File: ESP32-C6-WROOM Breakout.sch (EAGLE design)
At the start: 65 parts, among them J10 HP I2C, J11 LP I2C, J2 LP I2C, P1 GPIO-A2, P10 LP_I2C, P11 LiPo In, P2 GPIO-A1, P3 ADC, P4 O/P DRV, P5 CTRL, P6 HP_UART, P7 HP_I2C, P8 B2B-PH-K, P9 B2B-PH-K, U1 AP2112K-3.3TRG1, U2 ESP32-C6-WROOM-1-N4, U3 AP2112K-3.3TRG1LONG_PADS

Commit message: gitignore + WIP (close to candidate v1)
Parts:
- removed Q1, Q2, Q3, Q4: (no value), Master 2016:MOSFET-P-SOT23
- removed U1: AP2112K-3.3TRG1, AP2112K-3.3TRG1:AP2112K-3.3TRG1
- added J3: HP_UART, Connector:HEADER-5P-2.54
- added Q6, Q7, Q8: (no value), Master 2016:FDN338P_PMOSSOT23_LONG
- U3: value AP2112K-3.3TRG1LONG_PADS -> AP2112
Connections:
- net GND: now also J3.1; no longer U1.GND
- net GPIO22: now also Q8.G; no longer Q2.G
- net GPIO23: now also Q6.G; no longer Q4.G
- net LP_GPIO4: now also Q7.G; no longer Q3.G
- net LP_GPIO5: no longer Q1.G
- net N$12: now also Q7.D; no longer Q3.D
- net N$13: no longer U1.VOUT
- net N$15: now also Q6.D; no longer Q4.D
- net N$7: no longer Q1.D
- net RX: now also J3.4
- net TX: now also J3.5
- net UART_VCC: now also J3.3, Q8.D; no longer Q2.D
- net VCC: now also Q6.S, Q7.S, Q8.S; no longer Q1.S, Q2.S, Q3.S, Q4.S
- net VIN: no longer U1.EN, U1.VIN
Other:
- moved on the sheet: C6, C7, J10, P7, Q5, U3

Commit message: WIP getting there
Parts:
- added P12: Pwr Out, con-jst-ph:B3B-PH-K
- added P13: (no value), Master 2016:HEADER-1X2PPTH
- added Q1: FDN338P, Master 2016:FDN338P_PMOSSOT23_LONG
- added R12, R13, R14, R15, R21: (no value), Master 2016:R-EU_
- added R16, R17, R18, R19: 4k7, Master 2016:R-EU_
- added R20: 10k, Master 2016:R-EU_
- BAT1: value (none) -> 2-1775485-1
- C1, C2: value (none) -> 18p
- C3: value (none) -> 10u
- JP10: value BOOT -> (none)
- JP12: value (none) -> UART Vcc; device Master 2016:HEADER-1X2PPTH -> Connector:HEADER-3P-2.54
- JP8: value (none) -> BOOT
- JP9: value (none) -> I_measure
- P1: value GPIO-A2 -> LP_I2C; device con-jst-eh:B3B-EH-A -> con-jst-eh:B4B-EH-A
- P10: value LP_I2C -> Pwr Sw 23; device con-jst-eh:B4B-EH-A -> con-jst-ph:B2B-PH-K
- P2: value GPIO-A1 -> HP_I2C; device con-jst-eh:B5B-EH-A -> con-jst-eh:B4B-EH-A
- P3: value ADC -> CTRL
- P5: value CTRL -> ADC; device con-jst-eh:B3B-EH-A -> con-jst-eh:B4B-EH-A
- P6: value HP_UART -> GPIO-A1; device con-jst-eh:B4B-EH-A -> con-jst-eh:B5B-EH-A
- P7: value HP_I2C -> HP_UART
- P8: value B2B-PH-K -> GPIO-A2; device con-jst-ph:B2B-PH-K -> con-jst-eh:B3B-EH-A
- P9: value B2B-PH-K -> Pwr Sw 22
- Q5, Q6, Q7, Q8: value (none) -> FDN338P
- R3, R5, R6, R8: value (none) -> 10k
- X1: value (none) -> CFS-20632768EZFB
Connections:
- new net LP_GPIO6: U2.IO6
- new net LP_GPIO7: U2.IO7
- new net N$9: P5.4, Q1.D
- new net PWR_SW_22: JP12.P$1, JP6.2, P9.2, Q8.D
- net ADC: now also P5.2; no longer P3.2
- net GND: now also JP2.2, JP3.2, P1.2, P10.1, P12.1, P2.2, P7.1; no longer JP10.2, JP7.2, P1.1, P10.2, P2.1, P7.2
- net GPIO10: now also P2.3, R18.1; no longer P7.3
- net GPIO11: now also P2.4, R19.1; no longer P7.4
- net GPIO15_R: now also JP10.2, P3.2; no longer JP11.2, P5.2
- net GPIO18: now also P6.2; no longer P2.2
- net GPIO19: now also JP2.1, P6.3; no longer JP7.1, P2.3
- net GPIO20: now also JP3.1, P6.4; no longer JP8.1, P2.4
- net GPIO21: now also P6.5, R2.1; no longer P2.5
- net GPIO22: now also P8.3, R15.1, R15.2; no longer P1.3, R2.1
- net GPIO23: now also P8.2, R14.1, R14.2; no longer P1.2
- net GPIO6: now also P1.4, Q1.G, R16.2, R20.1, R21.1, R21.2; no longer P10.4, U2.IO6
- net GPIO7: now also P1.3, R17.2; no longer P10.3, U2.IO7
- net GPIO8: now also P13.1; no longer JP6.1
- net GPIO9: now also P13.2; no longer JP6.2
- net LP_GPIO3: now also P3.3; no longer P5.3
- net LP_GPIO4: now also R13.1, R13.2
- net LP_GPIO5: now also JP5.2, R12.1, R12.2; no longer JP2.2
- net LP_GPIO5_P: now also JP5.1; no longer JP2.1
- net N$1: now also JP8.1; no longer JP10.1
- net N$10: now also JP11.2; no longer JP12.2
- net N$11: now also JP11.1; no longer JP12.1
- net N$15: now also JP7.2, P10.2; no longer JP5.2, P9.2
- net N$8: now also JP10.1; no longer JP11.1
- net RX: now also P7.3; no longer P6.3
- net TX: now also P7.2; no longer P6.2
- net UART_VCC: now also JP12.P$2, P7.4; no longer JP3.2, P6.4, P8.2, Q8.D
- net VCC: now also JP12.P$3, JP6.1, JP7.1, P1.1, P12.2, P2.1, P5.3, Q1.S, R16.1, R17.1, R18.2, R19.2, R20.2; no longer JP3.1, JP5.1, P10.1, P3.3, P7.1
- net VIN: now also P12.3
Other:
- note added: "Alt MIC5504"
- note added: "Cut trace if gate series resistors R12-R14 required"
- note added: "For CR2032 coin cell"
- note added: "R1, R2 chosen to suit load I"
- note added: "R16-R19 I2C pull-ups Use if required. Typically 3k9 or 4k7"
- note added: "R4, R7 to suit load I"
- note added: "Vcc control for ADC and LP_I2C are mutually incompatible"
- note added: "see also LED1"
- note added: "see also P5"
- moved on the sheet: BAT1, C3, C6, C7, C8, D1, D3, J1, J10, J11, J2, J3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

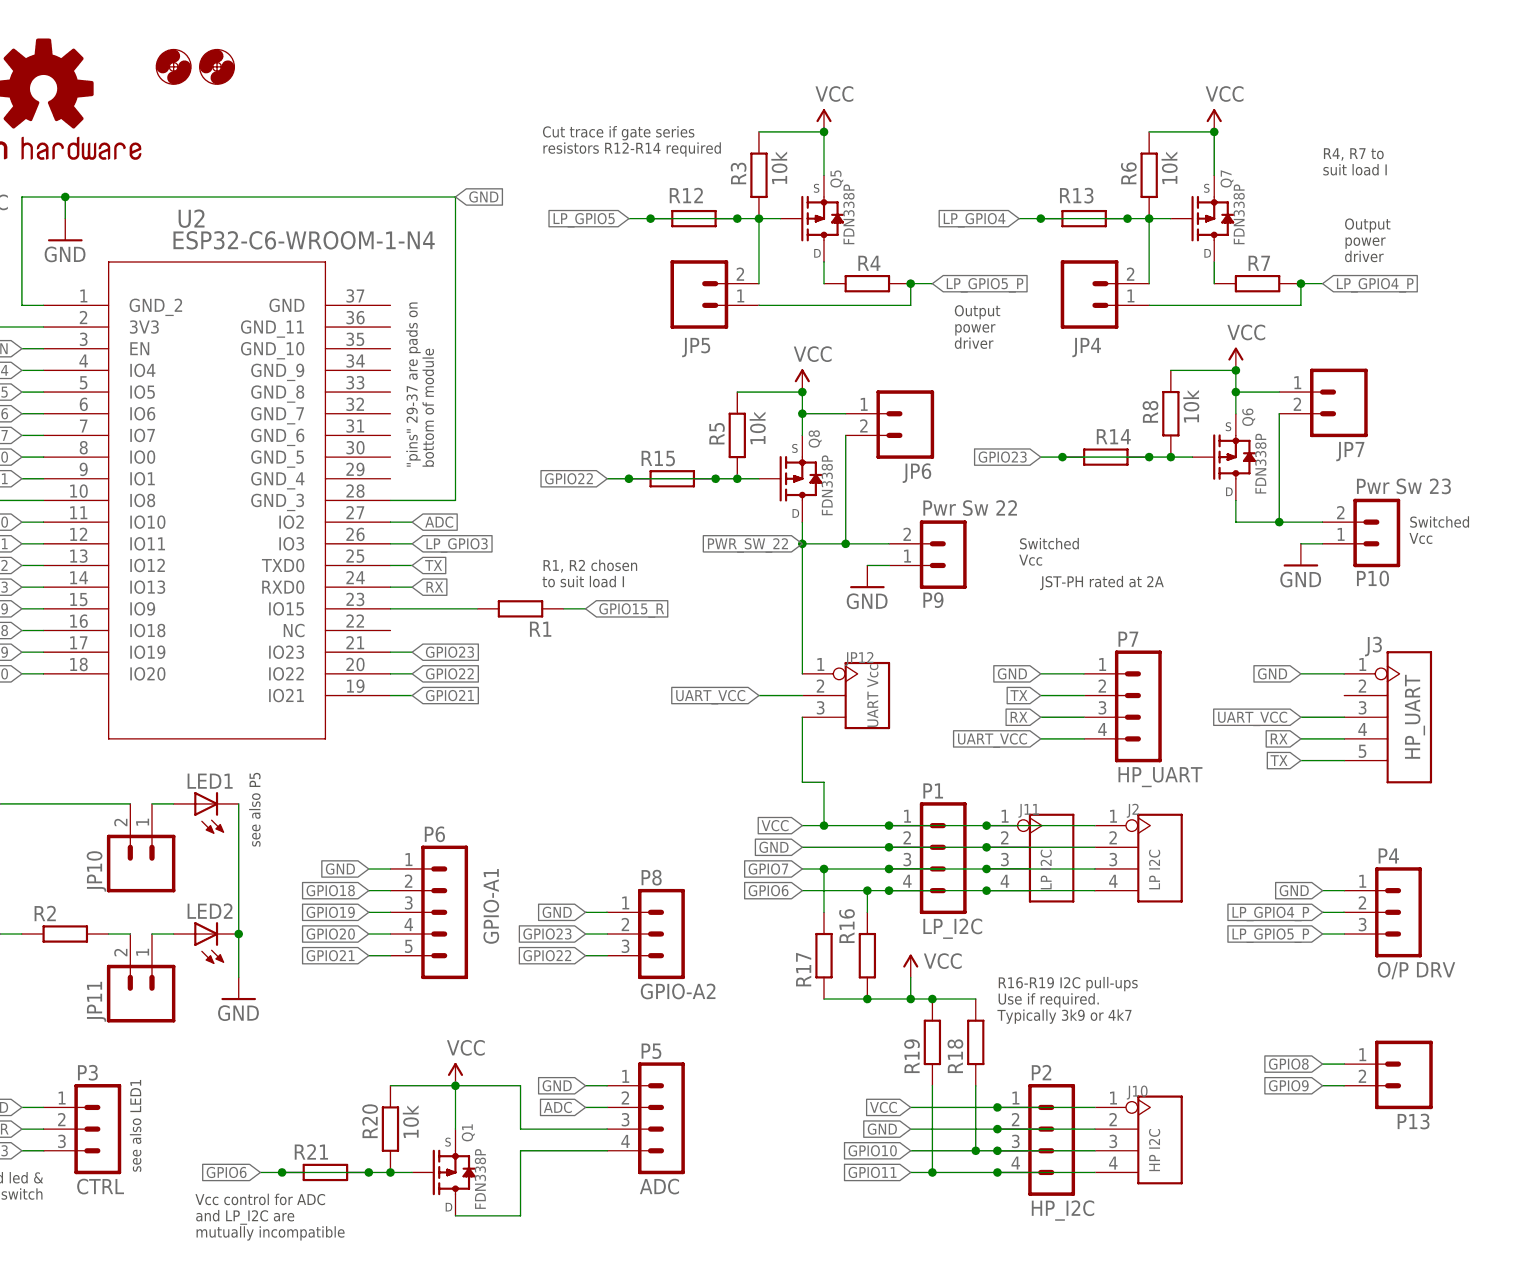
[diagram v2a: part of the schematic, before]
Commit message: move ADC and add o/p drive caps
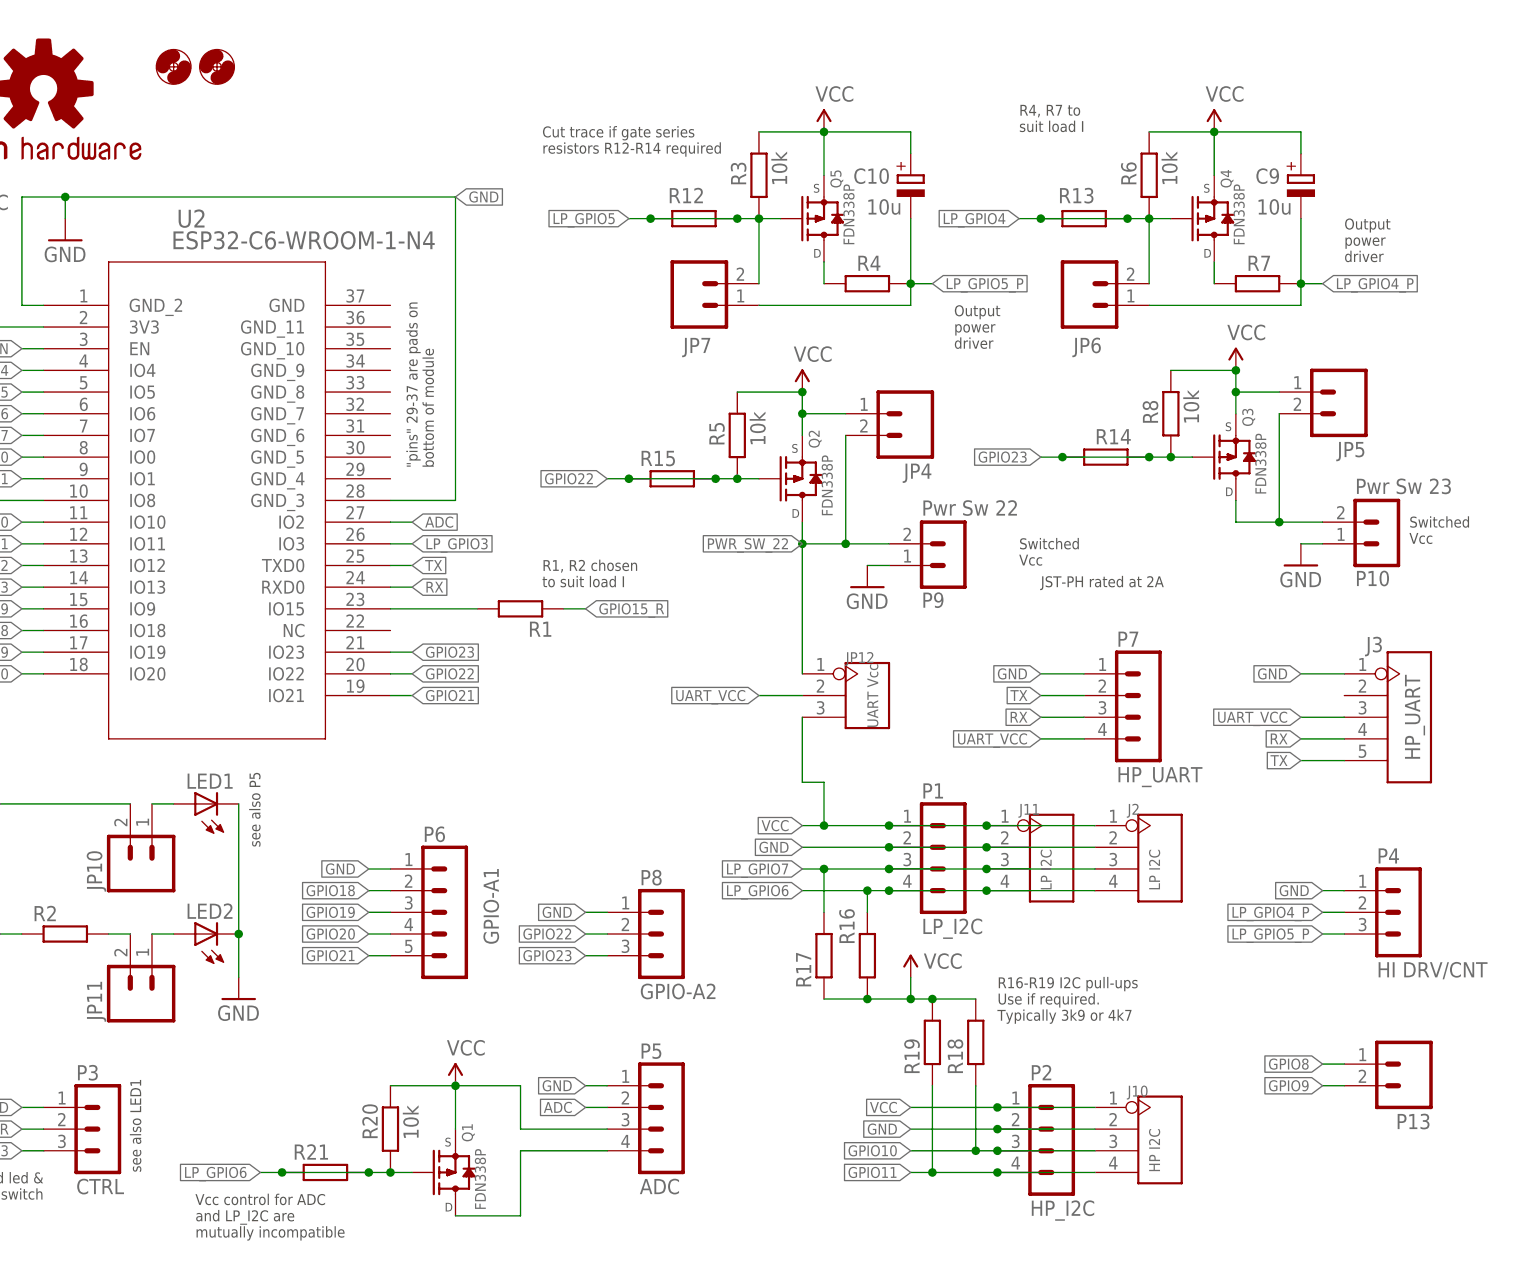
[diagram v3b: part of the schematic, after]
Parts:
- added C10, C9: 10u, Master 2016:CPOL-EUE2.5-5**10UF
- P4: value O/P DRV -> HI DRV/CNT
- renumbered Q6 to Q3, Q7 to Q4, Q8 to Q2
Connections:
- net N$16 renamed GPIO15
- removed net GPIO6: J11.P$4, J2.P$4, P1.4, Q1.G, R16.2, R20.1, R21.1, R21.2
- removed net GPIO7: J11.P$3, J2.P$3, P1.3, R17.2
- net GPIO22: now also P8.2; no longer P8.3
- net GPIO23: now also P8.3; no longer P8.2
- net LP_GPIO4: now also JP6.2; no longer JP4.2
- net LP_GPIO4_P: now also C9.-, JP6.1; no longer JP4.1
- net LP_GPIO5: now also JP7.2; no longer JP5.2
- net LP_GPIO5_P: now also C10.-, JP7.1; no longer JP5.1
- net LP_GPIO6: now also J11.P$4, J2.P$4, P1.4, Q1.G, R16.2, R20.1, R21.1, R21.2
- net LP_GPIO7: now also J11.P$3, J2.P$3, P1.3, R17.2
- net N$15: now also JP5.2; no longer JP7.2
- net PWR_SW_22: now also JP4.2; no longer JP6.2
- net VCC: now also C10.+, C9.+, JP4.1, JP5.1; no longer JP6.1, JP7.1
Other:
- moved on the sheet: JP4, JP5, JP6, JP7

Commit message: close to v1 rev
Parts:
- removed Q5: FDN338P, Master 2016:FDN338P_PMOSSOT23_LONG
- added D4: SL115B, Master 2016:DIODE-SCHOTTKY
- added J4, J5: (no value), Connector:HEADER-1P-35
- added JP13: PS Src, Connector:HEADER-3P-2.54
- added JP14: I_measure, Master 2016:HEADER-1X2PPTH
- added P14: Backup, con-jst-ph:B2B-PH-K
- C10: device Master 2016:CPOL-EUE2.5-5**10UF -> Master 2016:C-EU1206
- C3, C9: value 10u -> 100n; device Master 2016:CPOL-EUE2.5-5**10UF -> Master 2016:C-EU1206
- C6: value 100n -> 1u
- C7: value 10u -> 1u; device Master 2016:CPOL-EUE2.5-5**10UF -> Master 2016:C-EU1206
- C8: value 100n -> 10u
- J2: value LP I2C -> HP I2C
- JP3: value (none) -> BOOT
- JP8: value BOOT -> (none)
- JP9: value I_measure -> (none)
- P10: device con-jst-ph:B2B-PH-K -> con-jst-ph:B3B-PH-K
- P5: device con-jst-eh:B4B-EH-A -> con-jst-eh:B3B-EH-A
- P6: device con-jst-eh:B5B-EH-A -> con-jst-eh:B6B-EH-A
- R20: value 10k -> 2k2
- R21: value (none) -> 1k
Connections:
- new net N$14: JP13.P$3, P10.3
- new net N$16: J4.1, JP1.1
- new net N$2: D2.A, P11.1
- new net N$5: JP13.P$2, JP5.1, Q1.S, R8.2
- net ADC: now also C9.1, R20.1, R21.1
- net GND: now also C10.1, C3.2, C7.2, C9.2, P10.2, P11.2, P12.2, P14.2, P9.2, R20.2; no longer C3.-, C7.-, JP8.2, P10.1, P11.1, P12.1, P9.1
- net GPIO10: now also J2.P$3
- net GPIO11: now also J2.P$4
- net GPIO18: no longer JP1.1
- net GPIO19: no longer JP2.1
- net GPIO20: no longer JP3.1
- net GPIO23: now also Q1.G; no longer Q3.G
- net LP_GPIO4: now also Q3.G; no longer Q4.G
- net LP_GPIO4_P: now also JP8.2; no longer C9.-
- net LP_GPIO5: now also Q4.G; no longer Q5.G
- net LP_GPIO5_P: now also JP9.2; no longer C10.-
- net LP_GPIO6: no longer J2.P$4, Q1.G, R20.1, R21.1, R21.2
- net LP_GPIO7: no longer J2.P$3
- net N$1: now also JP3.1; no longer JP8.1
- net N$12: now also JP8.1, Q3.D; no longer Q4.D
- net N$13: now also C7.1, D3.C, JP14.1; no longer C6.1, C7.+, JP9.1
- net N$15: now also P10.1, Q1.D; no longer P10.2, Q3.D
- net N$4: now also D4.A, P14.1; no longer D2.A, P11.2
- net N$7: now also JP9.1, Q4.D; no longer Q5.D
- net N$9: now also J5.1, JP2.1; no longer P5.4, Q1.D
- net PWR_SW_22: now also P9.1; no longer P9.2
- net VCC: now also C10.2, C3.1, C8.1, JP13.P$1, JP14.2, P12.1, P6.6; no longer C10.+, C9.+, JP5.1, JP9.2, P12.2, Q1.S, Q5.S, R20.2, R8.2
- net VIN: now also C6.1, D4.C, R21.2; no longer C3.+, C8.1, D3.C
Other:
- note added: "Allow for an external Pwr src to be switched"
- note added: "C8 is decoupling for one/both"
- note added: "Config Jumpers not attached - use flying wires to link to GPIO"
- note added: "Output power driver. Not meant for PWM (MOSFET gate driver better at high freq)"
- note added: "P14 is option for e.g. a LiSOCl2 cell for when coin cell is insufficient."
- note added: "R4, R7 to suit load I. Parallel JP to allow easy changing."
- note added: "see also P3"
- note removed: "Config Jumpers"
- note removed: "Output power driver"
- note removed: "R4, R7 to suit load I"
- note removed: "Vcc control for ADC and LP_I2C are mutually incompatible"
- note removed: "see also P5"
- moved on the sheet: C6, C8, D3, J10, J2, J3, JP3, JP5, JP6, JP7, JP8, JP9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

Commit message: v1.1 essentially completed
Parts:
- removed JP10, JP4: (no value), Master 2016:HEADER-1X2PPTH
- removed JP13: PS Src, Connector:HEADER-3P-2.54
- removed Q4: FDN338P, Master 2016:FDN338P_PMOSSOT23_LONG
- added R22: 22k, Master 2016:R-EU_
- added U1: 74LVC1G3157, ESP32 Projects:SN74LVC1G3157DBVR
- added U4, U5: MIC2005A-1YM5, ESP32 Projects:MIC2005A-1YM5-TRSOT-23-5_M5_MCH-M
- added USB1: (no value), Master 2016:USB-FCI_SMD_LONG***
- J1: value (none) -> HP I2C; device Master 2016:USB-FCI_SMD*** -> Connector:HEADER-4P-80/40MIL
- J10: value HP I2C -> (none); device Connector:HEADER-4P-80/40MIL -> Master 2016:HEADER-1X2PPTH
- P10: device con-jst-ph:B3B-PH-K -> con-jst-ph:B2B-PH-K
- P11: value LiPo In -> Battery
- P13: value (none) -> Pwr Sw 22; device Master 2016:HEADER-1X2PPTH -> con-jst-ph:B2B-PH-K
- P5: value ADC -> ADC (ext batt)
- P9: value Pwr Sw 22 -> GPIO-B; device con-jst-ph:B2B-PH-K -> con-jst-eh:B4B-EH-A
- R15: value (none) -> 10k
- R20: value 2k2 -> 10k
- R21: value 1k -> 22k
- U2: value ESP32-C6-WROOM-1-N4 -> ESP32-C6-WROOM-1-N4LONG; device SMD Stamp Modules:ESP32-C6-WROOM-1-N4 -> SMD Stamp Modules:ESP32-C6-WROOM-1-N4LONG
- U3: value AP2112 -> RT9080-33
- renumbered JP12 to J12, JP14 to J14, JP6 to J6, JP7 to J7, JP8 to J8, JP9 to J9
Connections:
- removed net N$14: JP13.P$3, P10.3
- new net ADC_EXT: P5.2, U1.B1
- new net VIN_DIV: R20.1, R21.1, U1.B2
- net ADC: now also U1.A; no longer P5.2, R20.1, R21.1
- net GND: now also J1.P$2, P10.1, P11.1, P13.1, P14.1, R15.2, R5.2, U1.GND, U4.GND, U5.GND, USB1.GND; no longer J1.GND, J10.P$2, P10.2, P11.2, P14.2
- net GPIO10: now also J1.P$3; no longer J10.P$3
- net GPIO11: now also J1.P$4; no longer J10.P$4
- net GPIO12: now also USB1.D-; no longer J1.D-
- net GPIO13: now also USB1.D+; no longer J1.D+
- net GPIO15: now also R5.1, U1.S, U5.ENABLE
- net GPIO15_R: now also J10.2; no longer JP10.2
- net GPIO22: now also U4.ENABLE; no longer Q2.G, R15.2, R5.1
- net GPIO8: now also P9.3; no longer P13.1
- net GPIO9: now also P9.1; no longer P13.2
- net LP_GPIO3: now also R22.1
- net LP_GPIO4: now also P5.3, Q2.G; no longer Q3.G
- net LP_GPIO5: now also Q3.G; no longer Q4.G
- net N$12: now also Q2.D; no longer Q3.D
- net N$15: now also R21.2, U5.VOUT; no longer JP5.2, P10.1, Q1.D
- net N$2: now also P11.2; no longer P11.1
- net N$3: now also USB1.VBUS; no longer J1.VBUS
- net N$4: now also P14.2; no longer P14.1
- net N$5: now also JP5.2, P10.2, Q1.D; no longer JP13.P$2, JP5.1, Q1.S, R8.2
- net N$7: now also Q3.D; no longer Q4.D
- net N$8: now also J10.1; no longer JP10.1
- net PWR_SW_22: now also P13.2, U4.VOUT; no longer JP4.2, P9.1, Q2.D
- net VCC: now also J1.P$1, JP5.1, P9.4, Q1.S, R22.2, R8.2, U1.VCC, U4.VIN; no longer J10.P$1, JP13.P$1, JP4.1, P5.3, Q4.S, R5.2
- net VIN: now also U5.VIN; no longer R21.2
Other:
- note added: "Alt MIC5504 or AP2112 (but these have higher I_q)"
- note removed: "Allow for an external Pwr src to be switched"
- note removed: "Alt MIC5504"
- moved on the sheet: C10, P11, P13, P14, Q2, Q3, R1, R15, R20, R21, R5
